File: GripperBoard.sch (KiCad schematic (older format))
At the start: 20 parts

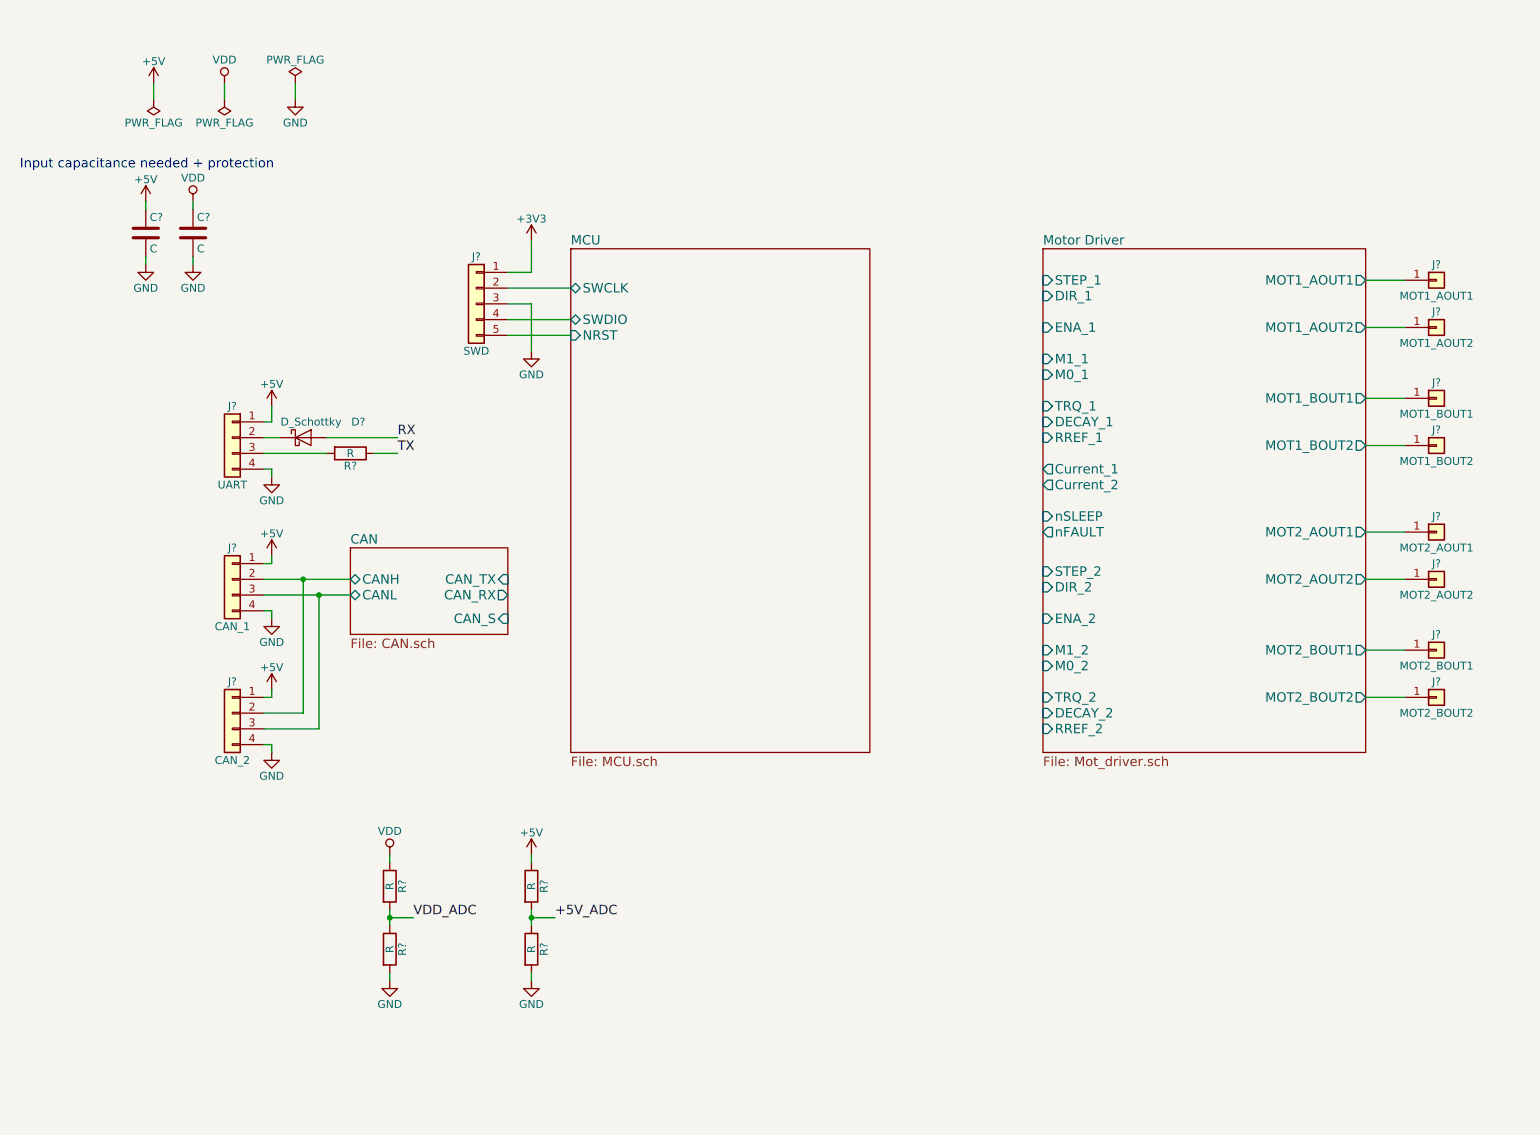
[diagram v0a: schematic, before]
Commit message: Finished schematic
Motordriver still needs footprint, it's necessary to choose new bulk capacitors
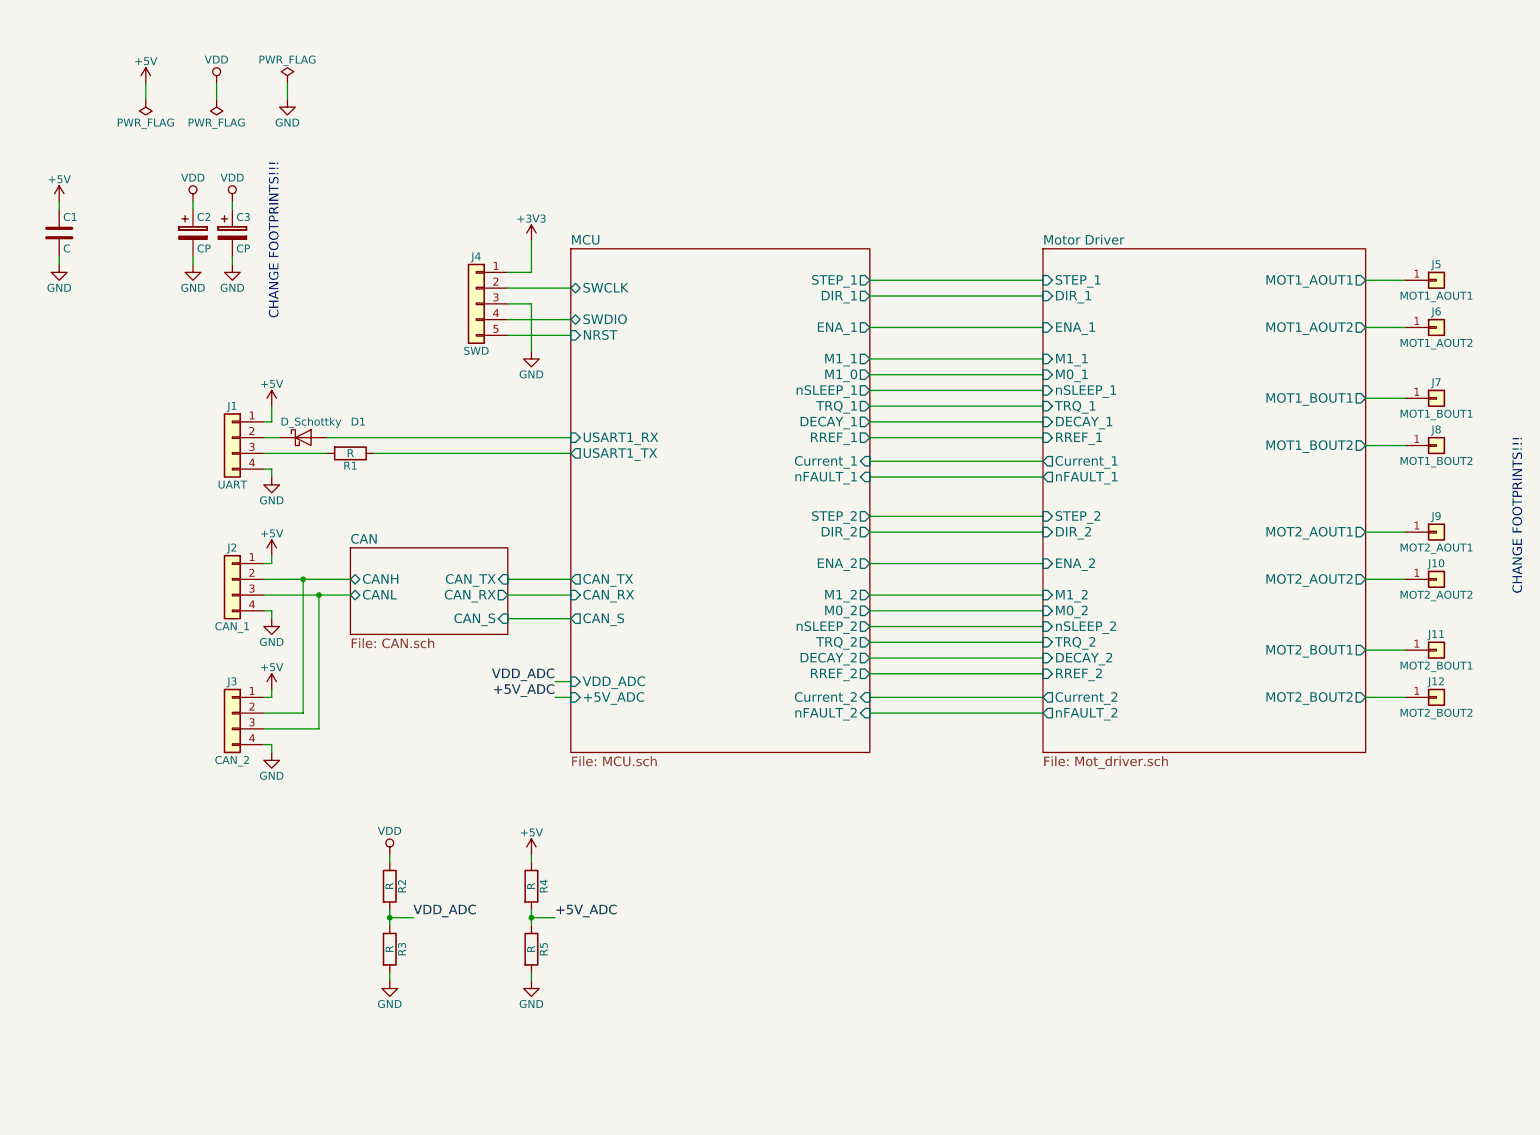
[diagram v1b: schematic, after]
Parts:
- removed C?: C, symbol C
- added C2, C3: CP, Capacitors_THT:CP_Axial_L11.0mm_D8.0mm_P15.00mm_Horizontal, symbol CP
- C1: renamed from C?; footprint (none) -> Capacitors_SMD:C_1206
- J10, J11, J12, J5, J6, J7, J8, J9: renamed from J?; footprint (none) -> Pin_Headers:Pin_Header_Straight_1x01_Pitch1.00mm
- R2, R3, R4, R5: renamed from R?; footprint (none) -> Resistors_SMD:R_0402
- gave numbers to parts that had none: 6
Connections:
- net GND: now also C2.2, C3.2
- net VDD: now also C2.1, C3.1
- net RX renamed MCU/USART1_RX
- net TX renamed MCU/USART1_TX
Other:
- note added: "CHANGE FOOTPRINTS!!!\n"
- note removed: "Input capacitance needed + protection"
- moved on the sheet: C1

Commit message: small updates
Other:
- note added: "CHANGE FOOTPRINTS\ndepending on the PCB design\n"
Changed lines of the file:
@@
 $EndComp
 $Comp
-L GND #PWR12
+L GND #PWR01
 U 1 1 5A133DFF
 P 2750 4550
-F 0 "#PWR12" H 2750 4300 50  0001 C CNN
+F 0 "#PWR01" H 2750 4300 50  0001 C CNN
 F 1 "GND" H 2750 4400 50  0000 C CNN
 F 2 "" H 2750 4550 50  0001 C CNN
@@
 $EndComp
 $Comp
-L GND #PWR14
+L GND #PWR02
 U 1 1 5A133FBF
 P 2750 5400
-F 0 "#PWR14" H 2750 5150 50  0001 C CNN
+F 0 "#PWR02" H 2750 5150 50  0001 C CNN
 F 1 "GND" H 2750 5250 50  0000 C CNN
 F 2 "" H 2750 5400 50  0001 C CNN
@@
 	2750 5350 2750 5400
 $Comp
-L +5V #PWR13
+L +5V #PWR03
 U 1 1 5A134174
 P 2750 5000
-F 0 "#PWR13" H 2750 4850 50  0001 C CNN
+F 0 "#PWR03" H 2750 4850 50  0001 C CNN
 F 1 "+5V" H 2750 5140 50  0000 C CNN
 F 2 "" H 2750 5000 50  0001 C CNN
@@
 $EndComp
 $Comp
-L +5V #PWR11
+L +5V #PWR04
 U 1 1 5A134334
 P 2750 4150
-F 0 "#PWR11" H 2750 4000 50  0001 C CNN
+F 0 "#PWR04" H 2750 4000 50  0001 C CNN
 F 1 "+5V" H 2750 4290 50  0000 C CNN
 F 2 "" H 2750 4150 50  0001 C CNN
@@
 Connection ~ 3050 4400
 $Comp
-L +3V3 #PWR18
+L +3V3 #PWR05
 U 1 1 5A14DFC5
 P 4400 2150
-F 0 "#PWR18" H 4400 2000 50  0001 C CNN
+F 0 "#PWR05" H 4400 2000 50  0001 C CNN
 F 1 "+3V3" H 4400 2290 50  0000 C CNN
 F 2 "" H 4400 2150 50  0001 C CNN
@@
 	4250 2750 4650 2750
 $Comp
-L GND #PWR19
+L GND #PWR06
 U 1 1 5A14EFC9
 P 4400 2850
-F 0 "#PWR19" H 4400 2600 50  0001 C CNN
+F 0 "#PWR06" H 4400 2600 50  0001 C CNN
 F 1 "GND" H 4400 2700 50  0000 C CNN
 F 2 "" H 4400 2850 50  0001 C CNN
@@
 $EndComp
 $Comp
-L GND #PWR17
+L GND #PWR07
 U 1 1 5A16790D
 P 3500 6850
-F 0 "#PWR17" H 3500 6600 50  0001 C CNN
+F 0 "#PWR07" H 3500 6600 50  0001 C CNN
 F 1 "GND" H 3500 6700 50  0000 C CNN
 F 2 "" H 3500 6850 50  0001 C CNN
@@
 $EndComp
 $Comp
-L VDD #PWR16
+L VDD #PWR08
 U 1 1 5A167BD9
 P 3500 6050
-F 0 "#PWR16" H 3500 5900 50  0001 C CNN
+F 0 "#PWR08" H 3500 5900 50  0001 C CNN
 F 1 "VDD" H 3500 6200 50  0000 C CNN
 F 2 "" H 3500 6050 50  0001 C CNN
@@
 	3500 6400 3500 6500
 $Comp
-L +5V #PWR20
+L +5V #PWR09
 U 1 1 5A168886
 P 4400 6050
-F 0 "#PWR20" H 4400 5900 50  0001 C CNN
+F 0 "#PWR09" H 4400 5900 50  0001 C CNN
 F 1 "+5V" H 4400 6190 50  0000 C CNN
 F 2 "" H 4400 6050 50  0001 C CNN
@@
 	4400 6400 4400 6500
 $Comp
-L GND #PWR21
+L GND #PWR010
 U 1 1 5A168C2F
 P 4400 6850
-F 0 "#PWR21" H 4400 6600 50  0001 C CNN
+F 0 "#PWR010" H 4400 6600 50  0001 C CNN
 F 1 "GND" H 4400 6700 50  0000 C CNN
 F 2 "" H 4400 6850 50  0001 C CNN
@@
 $EndComp
 $Comp
-L +5V #PWR9
+L +5V #PWR011
 U 1 1 5A175E15
 P 2750 3200
-F 0 "#PWR9" H 2750 3050 50  0001 C CNN
+F 0 "#PWR011" H 2750 3050 50  0001 C CNN
 F 1 "+5V" H 2750 3340 50  0000 C CNN
 F 2 "" H 2750 3200 50  0001 C CNN
@@
 	2750 3300 2750 3200
 $Comp
-L GND #PWR10
+L GND #PWR012
 U 1 1 5A175FA7
 P 2750 3650
-F 0 "#PWR10" H 2750 3400 50  0001 C CNN
+F 0 "#PWR012" H 2750 3400 50  0001 C CNN
 F 1 "GND" H 2750 3500 50  0000 C CNN
 F 2 "" H 2750 3650 50  0001 C CNN
@@
 	3400 3500 4650 3500
 $Comp
-L GND #PWR15
+L GND #PWR013
 U 1 1 5A1844F1
 P 2850 1250
-F 0 "#PWR15" H 2850 1000 50  0001 C CNN
+F 0 "#PWR013" H 2850 1000 50  0001 C CNN
 F 1 "GND" H 2850 1100 50  0000 C CNN
 F 2 "" H 2850 1250 50  0001 C CNN
@@
 $EndComp
 $Comp
-L VDD #PWR6
+L VDD #PWR014
 U 1 1 5A1845F1
 P 2400 1150
-F 0 "#PWR6" H 2400 1000 50  0001 C CNN
+F 0 "#PWR014" H 2400 1000 50  0001 C CNN
 F 1 "VDD" H 2400 1300 50  0000 C CNN
 F 2 "" H 2400 1150 50  0001 C CNN
@@
 $EndComp
 $Comp
-L PWR_FLAG #FLG3
+L PWR_FLAG #FLG015
 U 1 1 5A1847F1
 P 2850 1150
-F 0 "#FLG3" H 2850 1225 50  0001 C CNN
+F 0 "#FLG015" H 2850 1225 50  0001 C CNN
 F 1 "PWR_FLAG" H 2850 1300 50  0000 C CNN
 F 2 "" H 2850 1150 50  0001 C CNN
@@
 $EndComp
 $Comp
-L PWR_FLAG #FLG2
+L PWR_FLAG #FLG016
 U 1 1 5A184AD1
 P 2400 1250
-F 0 "#FLG2" H 2400 1325 50  0001 C CNN
+F 0 "#FLG016" H 2400 1325 50  0001 C CNN
 F 1 "PWR_FLAG" H 2400 1400 50  0000 C CNN
 F 2 "" H 2400 1250 50  0001 C CNN
@@
 	2400 1150 2400 1250
 $Comp
-L +5V #PWR1
+L +5V #PWR017
 U 1 1 5A1856D7
 P 1950 1150
-F 0 "#PWR1" H 1950 1000 50  0001 C CNN
+F 0 "#PWR017" H 1950 1000 50  0001 C CNN
 F 1 "+5V" H 1950 1290 50  0000 C CNN
 F 2 "" H 1950 1150 50  0001 C CNN
@@
 $EndComp
 $Comp
-L PWR_FLAG #FLG1
+L PWR_FLAG #FLG018
 U 1 1 5A185B88
 P 1950 1250
-F 0 "#FLG1" H 1950 1325 50  0001 C CNN
+F 0 "#FLG018" H 1950 1325 50  0001 C CNN
 F 1 "PWR_FLAG" H 1950 1400 50  0000 C CNN
 F 2 "" H 1950 1250 50  0001 C CNN
@@
 	9700 2400 9950 2400
 $Comp
-L +5V #PWR2
+L +5V #PWR019
 U 1 1 5A1912AB
 P 1400 1900
-F 0 "#PWR2" H 1400 1750 50  0001 C CNN
+F 0 "#PWR019" H 1400 1750 50  0001 C CNN
 F 1 "+5V" H 1400 2040 50  0000 C CNN
 F 2 "" H 1400 1900 50  0001 C CNN
@@
 	1400 1900 1400 1950
 $Comp
-L GND #PWR3
+L GND #PWR020
 U 1 1 5A191AF6
 P 1400 2300
-F 0 "#PWR3" H 1400 2050 50  0001 C CNN
+F 0 "#PWR020" H 1400 2050 50  0001 C CNN
 F 1 "GND" H 1400 2150 50  0000 C CNN
 F 2 "" H 1400 2300 50  0001 C CNN
@@
 	1400 2250 1400 2300
 $Comp
-L VDD #PWR4
+L VDD #PWR021
 U 1 1 5A191CCF
 P 2250 1900
-F 0 "#PWR4" H 2250 1750 50  0001 C CNN
+F 0 "#PWR021" H 2250 1750 50  0001 C CNN
 F 1 "VDD" H 2250 2050 50  0000 C CNN
 F 2 "" H 2250 1900 50  0001 C CNN
@@
 	2250 1900 2250 1950
 $Comp
-L GND #PWR5
+L GND #PWR022
 U 1 1 5A191FD3
 P 2250 2300
-F 0 "#PWR5" H 2250 2050 50  0001 C CNN
+F 0 "#PWR022" H 2250 2050 50  0001 C CNN
 F 1 "GND" H 2250 2150 50  0000 C CNN
 F 2 "" H 2250 2300 50  0001 C CNN
@@
 CHANGE FOOTPRINTS!!!\n
 $Comp
-L VDD #PWR7
+L VDD #PWR023
 U 1 1 5A151818
 P 2500 1900
-F 0 "#PWR7" H 2500 1750 50  0001 C CNN
+F 0 "#PWR023" H 2500 1750 50  0001 C CNN
 F 1 "VDD" H 2500 2050 50  0000 C CNN
 F 2 "" H 2500 1900 50  0001 C CNN
@@
 	2500 1900 2500 1950
 $Comp
-L GND #PWR8
+L GND #PWR024
 U 1 1 5A15181F
 P 2500 2300
-F 0 "#PWR8" H 2500 2050 50  0001 C CNN
+F 0 "#PWR024" H 2500 2050 50  0001 C CNN
 F 1 "GND" H 2500 2150 50  0000 C CNN
 F 2 "" H 2500 2300 50  0001 C CNN
@@
 	1    0    0    -1
 $EndComp
-Text Notes 2800 2650 1    60   ~ 0
-CHANGE FOOTPRINTS!!!\n
+Text Notes 3050 2750 2    60   ~ 0
+CHANGE FOOTPRINTS\ndepending on the PCB design\n
 $EndSCHEMATC

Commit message: udated schematics
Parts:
- C1: value C -> 100u 6V3; footprint Capacitors_SMD:C_1206 -> Capacitors_SMD:C_0805
- C2, C3: value CP -> 16V CP
- R1: value R -> 100R
- R2: value R -> 150k
- R3, R4, R5: value R -> 33k
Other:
- moved on the sheet: C2
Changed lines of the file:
@@
 $EndComp
 $Comp
-L GND #PWR01
+L GND #PWR12
 U 1 1 5A133DFF
 P 2750 4550
-F 0 "#PWR01" H 2750 4300 50  0001 C CNN
+F 0 "#PWR12" H 2750 4300 50  0001 C CNN
 F 1 "GND" H 2750 4400 50  0000 C CNN
 F 2 "" H 2750 4550 50  0001 C CNN
@@
 $EndComp
 $Comp
-L GND #PWR02
+L GND #PWR14
 U 1 1 5A133FBF
 P 2750 5400
-F 0 "#PWR02" H 2750 5150 50  0001 C CNN
+F 0 "#PWR14" H 2750 5150 50  0001 C CNN
 F 1 "GND" H 2750 5250 50  0000 C CNN
 F 2 "" H 2750 5400 50  0001 C CNN
@@
 	2750 5350 2750 5400
 $Comp
-L +5V #PWR03
+L +5V #PWR13
 U 1 1 5A134174
 P 2750 5000
-F 0 "#PWR03" H 2750 4850 50  0001 C CNN
+F 0 "#PWR13" H 2750 4850 50  0001 C CNN
 F 1 "+5V" H 2750 5140 50  0000 C CNN
 F 2 "" H 2750 5000 50  0001 C CNN
@@
 $EndComp
 $Comp
-L +5V #PWR04
+L +5V #PWR11
 U 1 1 5A134334
 P 2750 4150
-F 0 "#PWR04" H 2750 4000 50  0001 C CNN
+F 0 "#PWR11" H 2750 4000 50  0001 C CNN
 F 1 "+5V" H 2750 4290 50  0000 C CNN
 F 2 "" H 2750 4150 50  0001 C CNN
@@
 Connection ~ 3050 4400
 $Comp
-L +3V3 #PWR05
+L +3V3 #PWR18
 U 1 1 5A14DFC5
 P 4400 2150
-F 0 "#PWR05" H 4400 2000 50  0001 C CNN
+F 0 "#PWR18" H 4400 2000 50  0001 C CNN
 F 1 "+3V3" H 4400 2290 50  0000 C CNN
 F 2 "" H 4400 2150 50  0001 C CNN
@@
 	4250 2750 4650 2750
 $Comp
-L GND #PWR06
+L GND #PWR19
 U 1 1 5A14EFC9
 P 4400 2850
-F 0 "#PWR06" H 4400 2600 50  0001 C CNN
+F 0 "#PWR19" H 4400 2600 50  0001 C CNN
 F 1 "GND" H 4400 2700 50  0000 C CNN
 F 2 "" H 4400 2850 50  0001 C CNN
@@
 P 3500 6250
 F 0 "R2" V 3580 6250 50  0000 C CNN
-F 1 "R" V 3500 6250 50  0000 C CNN
+F 1 "150k" V 3500 6250 50  0000 C CNN
 F 2 "Resistors_SMD:R_0402" V 3430 6250 50  0001 C CNN
 F 3 "" H 3500 6250 50  0001 C CNN
@@
 P 3500 6650
 F 0 "R3" V 3580 6650 50  0000 C CNN
-F 1 "R" V 3500 6650 50  0000 C CNN
+F 1 "33k" V 3500 6650 50  0000 C CNN
 F 2 "Resistors_SMD:R_0402" V 3430 6650 50  0001 C CNN
 F 3 "" H 3500 6650 50  0001 C CNN
@@
 $EndComp
 $Comp
-L GND #PWR07
+L GND #PWR17
 U 1 1 5A16790D
 P 3500 6850
-F 0 "#PWR07" H 3500 6600 50  0001 C CNN
+F 0 "#PWR17" H 3500 6600 50  0001 C CNN
 F 1 "GND" H 3500 6700 50  0000 C CNN
 F 2 "" H 3500 6850 50  0001 C CNN
@@
 $EndComp
 $Comp
-L VDD #PWR08
+L VDD #PWR16
 U 1 1 5A167BD9
 P 3500 6050
-F 0 "#PWR08" H 3500 5900 50  0001 C CNN
+F 0 "#PWR16" H 3500 5900 50  0001 C CNN
 F 1 "VDD" H 3500 6200 50  0000 C CNN
 F 2 "" H 3500 6050 50  0001 C CNN
@@
 	3500 6400 3500 6500
 $Comp
-L +5V #PWR09
+L +5V #PWR20
 U 1 1 5A168886
 P 4400 6050
-F 0 "#PWR09" H 4400 5900 50  0001 C CNN
+F 0 "#PWR20" H 4400 5900 50  0001 C CNN
 F 1 "+5V" H 4400 6190 50  0000 C CNN
 F 2 "" H 4400 6050 50  0001 C CNN
@@
 P 4400 6250
 F 0 "R4" V 4480 6250 50  0000 C CNN
-F 1 "R" V 4400 6250 50  0000 C CNN
+F 1 "33k" V 4400 6250 50  0000 C CNN
 F 2 "Resistors_SMD:R_0402" V 4330 6250 50  0001 C CNN
 F 3 "" H 4400 6250 50  0001 C CNN
@@
 P 4400 6650
 F 0 "R5" V 4480 6650 50  0000 C CNN
-F 1 "R" V 4400 6650 50  0000 C CNN
+F 1 "33k" V 4400 6650 50  0000 C CNN
 F 2 "Resistors_SMD:R_0402" V 4330 6650 50  0001 C CNN
 F 3 "" H 4400 6650 50  0001 C CNN
@@
 	4400 6400 4400 6500
 $Comp
-L GND #PWR010
+L GND #PWR21
 U 1 1 5A168C2F
 P 4400 6850
-F 0 "#PWR010" H 4400 6600 50  0001 C CNN
+F 0 "#PWR21" H 4400 6600 50  0001 C CNN
 F 1 "GND" H 4400 6700 50  0000 C CNN
 F 2 "" H 4400 6850 50  0001 C CNN
@@
 $EndComp
 $Comp
-L +5V #PWR011
+L +5V #PWR9
 U 1 1 5A175E15
 P 2750 3200
-F 0 "#PWR011" H 2750 3050 50  0001 C CNN
+F 0 "#PWR9" H 2750 3050 50  0001 C CNN
 F 1 "+5V" H 2750 3340 50  0000 C CNN
 F 2 "" H 2750 3200 50  0001 C CNN
@@
 	2750 3300 2750 3200
 $Comp
-L GND #PWR012
+L GND #PWR10
 U 1 1 5A175FA7
 P 2750 3650
-F 0 "#PWR012" H 2750 3400 50  0001 C CNN
+F 0 "#PWR10" H 2750 3400 50  0001 C CNN
 F 1 "GND" H 2750 3500 50  0000 C CNN
 F 2 "" H 2750 3650 50  0001 C CNN
@@
 P 3250 3500
 F 0 "R1" V 3330 3500 50  0000 C CNN
-F 1 "R" V 3250 3500 50  0000 C CNN
+F 1 "100R" V 3250 3500 50  0000 C CNN
 F 2 "Resistors_SMD:R_0402" V 3180 3500 50  0001 C CNN
 F 3 "" H 3250 3500 50  0001 C CNN
@@
 	3400 3500 4650 3500
 $Comp
-L GND #PWR013
+L GND #PWR15
 U 1 1 5A1844F1
 P 2850 1250
-F 0 "#PWR013" H 2850 1000 50  0001 C CNN
+F 0 "#PWR15" H 2850 1000 50  0001 C CNN
 F 1 "GND" H 2850 1100 50  0000 C CNN
 F 2 "" H 2850 1250 50  0001 C CNN
@@
 $EndComp
 $Comp
-L VDD #PWR014
+L VDD #PWR6
 U 1 1 5A1845F1
 P 2400 1150
-F 0 "#PWR014" H 2400 1000 50  0001 C CNN
+F 0 "#PWR6" H 2400 1000 50  0001 C CNN
 F 1 "VDD" H 2400 1300 50  0000 C CNN
 F 2 "" H 2400 1150 50  0001 C CNN
@@
 $EndComp
 $Comp
-L PWR_FLAG #FLG015
+L PWR_FLAG #FLG3
 U 1 1 5A1847F1
 P 2850 1150
-F 0 "#FLG015" H 2850 1225 50  0001 C CNN
+F 0 "#FLG3" H 2850 1225 50  0001 C CNN
 F 1 "PWR_FLAG" H 2850 1300 50  0000 C CNN
 F 2 "" H 2850 1150 50  0001 C CNN
@@
 $EndComp
 $Comp
-L PWR_FLAG #FLG016
+L PWR_FLAG #FLG2
 U 1 1 5A184AD1
 P 2400 1250
-F 0 "#FLG016" H 2400 1325 50  0001 C CNN
+F 0 "#FLG2" H 2400 1325 50  0001 C CNN
 F 1 "PWR_FLAG" H 2400 1400 50  0000 C CNN
 F 2 "" H 2400 1250 50  0001 C CNN
@@
 	2400 1150 2400 1250
 $Comp
-L +5V #PWR017
+L +5V #PWR3
 U 1 1 5A1856D7
 P 1950 1150
-F 0 "#PWR017" H 1950 1000 50  0001 C CNN
+F 0 "#PWR3" H 1950 1000 50  0001 C CNN
 F 1 "+5V" H 1950 1290 50  0000 C CNN
 F 2 "" H 1950 1150 50  0001 C CNN
@@
 $EndComp
 $Comp
-L PWR_FLAG #FLG018
+L PWR_FLAG #FLG1
 U 1 1 5A185B88
 P 1950 1250
-F 0 "#FLG018" H 1950 1325 50  0001 C CNN
+F 0 "#FLG1" H 1950 1325 50  0001 C CNN
 F 1 "PWR_FLAG" H 1950 1400 50  0000 C CNN
 F 2 "" H 1950 1250 50  0001 C CNN
@@
 	9700 2400 9950 2400
 $Comp
-L +5V #PWR019
+L +5V #PWR1
 U 1 1 5A1912AB
 P 1400 1900
-F 0 "#PWR019" H 1400 1750 50  0001 C CNN
+F 0 "#PWR1" H 1400 1750 50  0001 C CNN
 F 1 "+5V" H 1400 2040 50  0000 C CNN
 F 2 "" H 1400 1900 50  0001 C CNN
@@
 P 1400 2100
 F 0 "C1" H 1425 2200 50  0000 L CNN
-F 1 "C" H 1425 2000 50  0000 L CNN
-F 2 "Capacitors_SMD:C_1206" H 1438 1950 50  0001 C CNN
+F 1 "100u 6V3" V 1600 1950 50  0000 L CNN
+F 2 "Capacitors_SMD:C_0805" H 1438 1950 50  0001 C CNN
 F 3 "" H 1400 2100 50  0001 C CNN
 	1    1400 2100
@@
 	1400 1900 1400 1950
 $Comp
-L GND #PWR020
+L GND #PWR2
 U 1 1 5A191AF6
 P 1400 2300
-F 0 "#PWR020" H 1400 2050 50  0001 C CNN
+F 0 "#PWR2" H 1400 2050 50  0001 C CNN
 F 1 "GND" H 1400 2150 50  0000 C CNN
 F 2 "" H 1400 2300 50  0001 C CNN
@@
 	1400 2250 1400 2300
 $Comp
-L VDD #PWR021
+L VDD #PWR4
 U 1 1 5A191CCF
-P 2250 1900
-F 0 "#PWR021" H 2250 1750 50  0001 C CNN
-F 1 "VDD" H 2250 2050 50  0000 C CNN
-F 2 "" H 2250 1900 50  0001 C CNN
-F 3 "" H 2250 1900 50  0001 C CNN
-	1    2250 1900
-	1    0    0    -1
-$EndComp
-Wire Wire Line
-	2250 1900 2250 1950
-$Comp
-L GND #PWR022
+P 2100 1900
+F 0 "#PWR4" H 2100 1750 50  0001 C CNN
+F 1 "VDD" H 2100 2050 50  0000 C CNN
+F 2 "" H 2100 1900 50  0001 C CNN
+F 3 "" H 2100 1900 50  0001 C CNN
+	1    2100 1900
+	1    0    0    -1
+$EndComp
+Wire Wire Line
+	2100 1900 2100 1950
+$Comp
+L GND #PWR5
 U 1 1 5A191FD3
-P 2250 2300
-F 0 "#PWR022" H 2250 2050 50  0001 C CNN
-F 1 "GND" H 2250 2150 50  0000 C CNN
-F 2 "" H 2250 2300 50  0001 C CNN
-F 3 "" H 2250 2300 50  0001 C CNN
-	1    2250 2300
-	1    0    0    -1
-$EndComp
-Wire Wire Line
-	2250 2250 2250 2300
+P 2100 2300
+F 0 "#PWR5" H 2100 2050 50  0001 C CNN
+F 1 "GND" H 2100 2150 50  0000 C CNN
+F 2 "" H 2100 2300 50  0001 C CNN
+F 3 "" H 2100 2300 50  0001 C CNN
+	1    2100 2300
+	1    0    0    -1
+$EndComp
+Wire Wire Line
+	2100 2250 2100 2300
 Wire Wire Line
 	4250 4300 4650 4300
@@
 L CP C2
 U 1 1 5A20155E
-P 2250 2100
-F 0 "C2" H 2275 2200 50  0000 L CNN
-F 1 "CP" H 2275 2000 50  0000 L CNN
-F 2 "Capacitors_THT:CP_Axial_L11.0mm_D8.0mm_P15.00mm_Horizontal" H 2288 1950 50  0001 C CNN
-F 3 "" H 2250 2100 50  0001 C CNN
-	1    2250 2100
+P 2100 2100
+F 0 "C2" H 2125 2200 50  0000 L CNN
+F 1 "16V CP" V 2300 2000 50  0000 L CNN
+F 2 "Capacitors_THT:CP_Axial_L11.0mm_D8.0mm_P15.00mm_Horizontal" H 2138 1950 50  0001 C CNN
+F 3 "" H 2100 2100 50  0001 C CNN
+	1    2100 2100
 	1    0    0    -1
 $EndComp
@@
 CHANGE FOOTPRINTS!!!\n
 $Comp
-L VDD #PWR023
+L VDD #PWR7
 U 1 1 5A151818
 P 2500 1900
-F 0 "#PWR023" H 2500 1750 50  0001 C CNN
+F 0 "#PWR7" H 2500 1750 50  0001 C CNN
 F 1 "VDD" H 2500 2050 50  0000 C CNN
 F 2 "" H 2500 1900 50  0001 C CNN
@@
 	2500 1900 2500 1950
 $Comp
-L GND #PWR024
+L GND #PWR8
 U 1 1 5A15181F
 P 2500 2300
-F 0 "#PWR024" H 2500 2050 50  0001 C CNN
+F 0 "#PWR8" H 2500 2050 50  0001 C CNN
 F 1 "GND" H 2500 2150 50  0000 C CNN
 F 2 "" H 2500 2300 50  0001 C CNN
@@
 P 2500 2100
 F 0 "C3" H 2525 2200 50  0000 L CNN
-F 1 "CP" H 2525 2000 50  0000 L CNN
+F 1 "16V CP" V 2700 2000 50  0000 L CNN
 F 2 "Capacitors_THT:CP_Axial_L11.0mm_D8.0mm_P15.00mm_Horizontal" H 2538 1950 50  0001 C CNN
 F 3 "" H 2500 2100 50  0001 C CNN
